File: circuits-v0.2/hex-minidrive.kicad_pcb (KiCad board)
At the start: 2 copper layers, 32 x 64 mm, 101 parts, among them P1 2P 2.54mm header, X1 16MHz

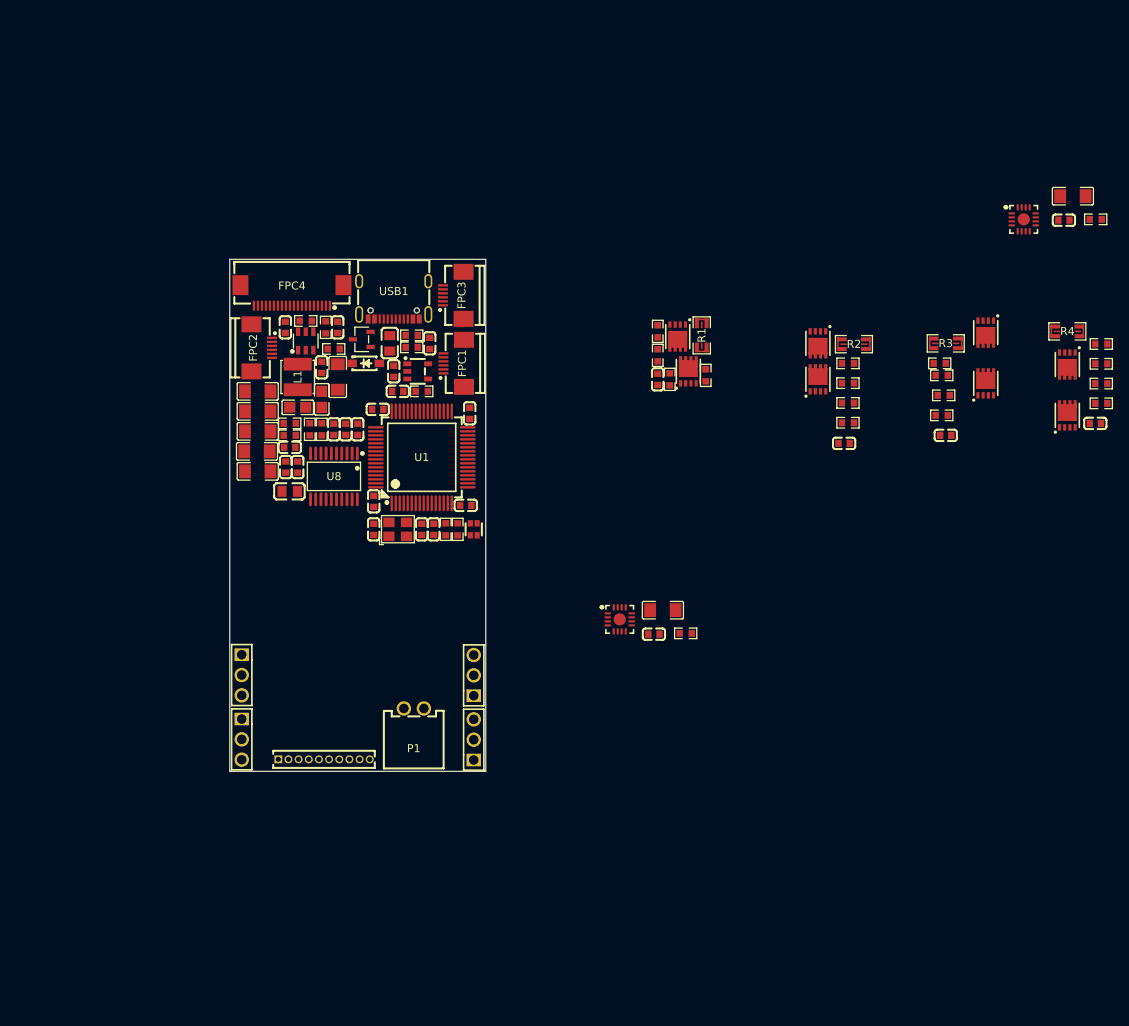
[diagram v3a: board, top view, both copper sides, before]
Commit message: Near final v0.2 circuit design.
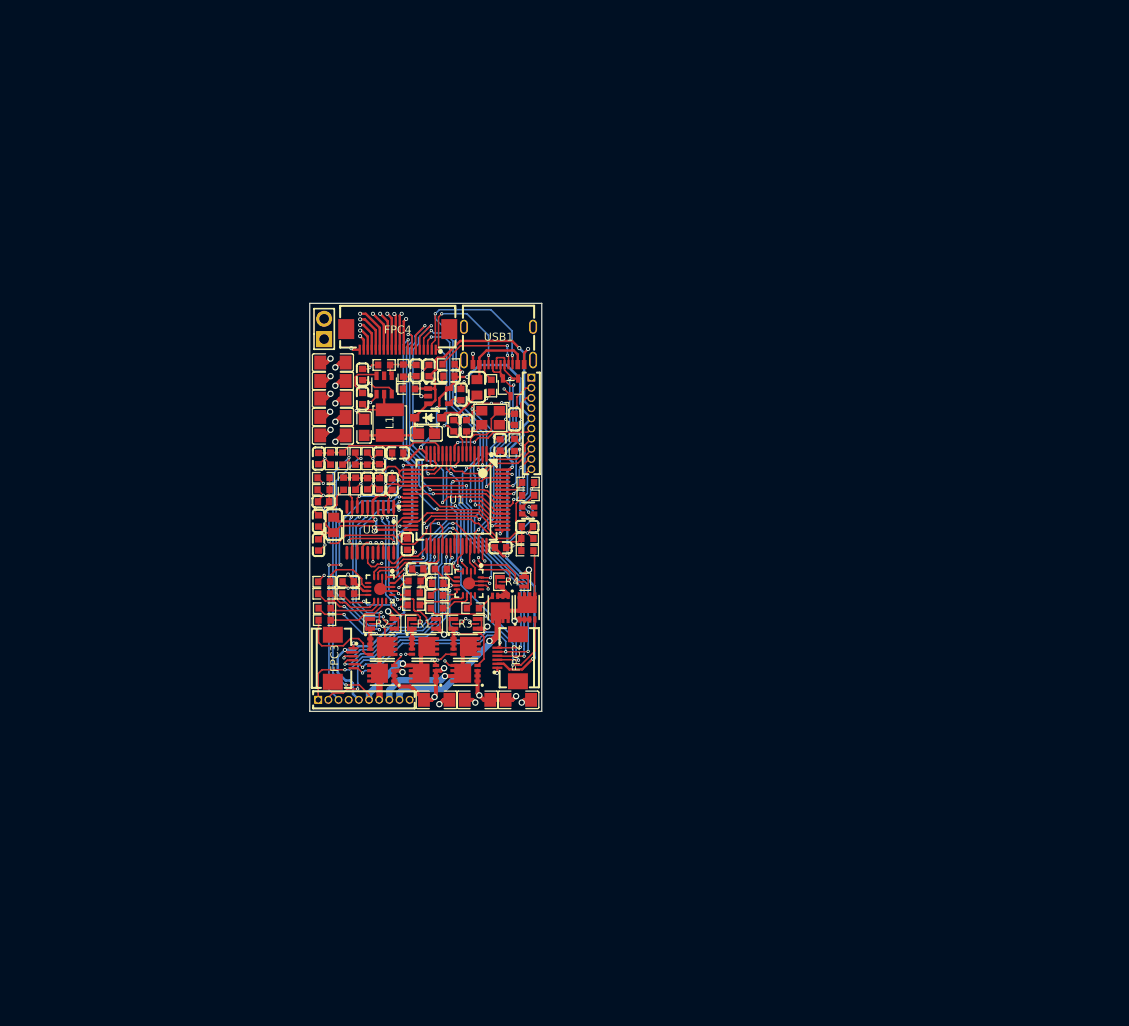
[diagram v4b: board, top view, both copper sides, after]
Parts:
- removed C502, C602: 100nF, Library:C0603
- removed FPC1: ~, Library:FPC-SMD_6P-P0.50_XUNPU_FPC-05F-6PH20
- removed H4: 2.54mm 3P header, Library:HDR-TH_3P-P2.54-V-M-1
- removed H5: 10P 1.27mm header, Library:HDR-TH_HX-PZ1.27-1X10P-ZZ
- removed P1: 2P 2.54mm header, Library:CONN-TH_2P-P2.50_XH-2AW
- added C17: 10uF, Library:C1206, F.Cu at (58.9, 60.7)
- added C18: 10uF, Library:C1206, F.Cu at (58.9, 63.0)
- C501, C601: value 10uF -> 100nF; footprint Library:C1206 -> Library:C0603
- H1, H3: value 2.54mm 3P header -> 10P 1.27mm header; footprint Library:HDR-TH_3P-P2.54-V-M-1 -> Library:HDR-TH_HX-PZ1.27-1X10P-ZZ
- H2: value 2.54mm 3P header -> 2P-2.54mm-header; footprint Library:HDR-TH_3P-P2.54-V-M-1 -> Library:HDR-TH_2P-P2.54-V-M
- moved C601 93.0 mm to (72.0, 81.5)
- moved R601 92.8 mm to (72.4, 79.7)
- moved R402 88.5 mm to (71.9, 84.6)
- moved R401 85.2 mm to (76.4, 84.6)
- moved U6 82.9 mm to (75.9, 81.5), turned to -90 degrees
- moved Q7 77.1 mm to (79.8, 84.6)
- moved R4 76.1 mm to (81.3, 81.3)
- moved Q5 75.9 mm to (75.5, 89.4), turned to -90 degrees
- moved R403 74.7 mm to (83.2, 77.4)
- moved Q6 74.4 mm to (75.5, 92.7), turned to 90 degrees
- moved R404 73.7 mm to (83.2, 75.9), turned to 180 degrees
- moved R201 72.9 mm to (57.9, 86.1), turned to 180 degrees
- moved R301 72.4 mm to (69.0, 84.2), turned to 180 degrees
- moved C401 72.2 mm to (83.2, 74.4), turned to 180 degrees
- moved Q8 71.7 mm to (83.2, 84.5)
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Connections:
- net Net-(U1-PF0-OSC_IN) renamed /OSC1
- net Net-(U1-PF1-OSC_OUT) renamed /OSC2
- net Net-(U5-VCC1) renamed /Driver1-internal-LDO
- net Net-(U6-VCC1) renamed /Driver2-internal-LDO
- H1 pad 1: 3V3 -> TIM3_CH1/ENCODER_1
- H1 pad 2: ADC1_IN7/POT_1 -> TIM3_CH2/ENCODER_2
- H1 pad 3: GND -> TIM3_CH3/ENCODER_3
- H2 pad 1: 3V3 -> VCC
- H2 pad 2: ADC1_IN8/POT_2 -> GND
- H3 pad 1: 3V3 -> GND
- H3 pad 2: ADC2_IN17/POT_3 -> SYS_JTCK-SWCLK
- H3 pad 3: GND -> SYS_JTMS-SVDIO
- U5 pad 17: unconnected-(U5-EP-Pad17) -> GND
- U6 pad 17: unconnected-(U6-EP-Pad17) -> GND
- USB1 pad A8: unconnected-(USB1-SBU1-PadA8) -> NRST
- USB1 pad B8: unconnected-(USB1-SBU2-PadB8) -> BOOT0/STOP
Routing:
- net 3V3: track 0.00 -> 143.5 mm, vias 0 -> 13
- net GND: track 0.00 -> 123.3 mm, vias 0 -> 64
- net VCC: track 0.00 -> 68.4 mm, vias 0 -> 22
- net FREE_IO_1: track 0.00 -> 54.5 mm, vias 0 -> 4
- net FREE_IO_2: track 0.00 -> 52.9 mm, vias 0 -> 4
- net M1: track 0.00 -> 48.0 mm, vias 0 -> 3
- net BOOT0/STOP: track 0.00 -> 46.3 mm, vias 0 -> 3
- net ADC1_IN3/HALF_3V3_REF: track 0.00 -> 40.7 mm, vias 0 -> 4
- net 5V: track 0.00 -> 40.5 mm, vias 0 -> 1
- net SPI3_MOSI: track 0.00 -> 37.2 mm, vias 0 -> 2
- net M2: track 0.00 -> 36.7 mm, vias 0 -> 2
- net SPI3_MISO: track 0.00 -> 35.3 mm, vias 0 -> 2
- net I2C2_SCL: track 0.00 -> 34.9 mm, vias 0 -> 2
- net TIM3_CH3/ENCODER_3: track 0.00 -> 34.5 mm, vias 0 -> 3
- net SPI3_SCK: track 0.00 -> 33.8 mm, vias 0 -> 2
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- added copper zone on In1.Cu, net GND
- added copper zone on In2.Cu, net VCC
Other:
- board size 32 x 64 mm -> 29 x 51 mm
- copper layers 2 -> 4
- board text added: "GND SWCLK SVDIO 5V 3V3 POT1 POT2 POT3 TOOL DIR"
- board text added: "GND VCC"
- board text added: "H1 H2 H3 GND 3V3 M1 M2 M3 M4 X"
- board text added: "IO2 IO1 I2C2_SCL I2C2_SDA 3V3 GND"
- board text added: "IO2 IO1 I2C3_SCL I2C3_SDA 3V3 GND"
